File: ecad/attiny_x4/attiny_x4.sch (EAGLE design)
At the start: 1 part

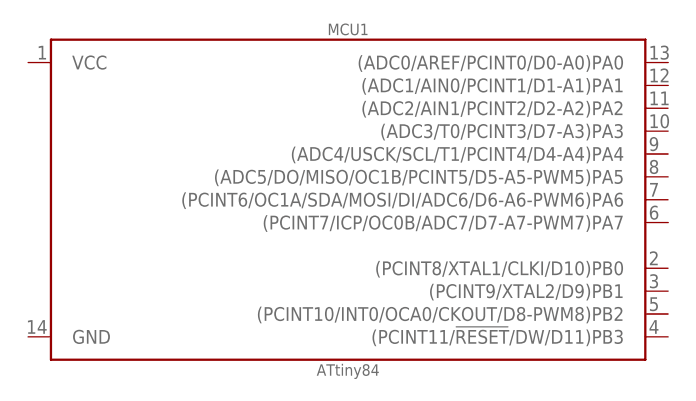
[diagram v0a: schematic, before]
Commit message: Update ATtiny84 symbol to match the CCW ATtiny core.
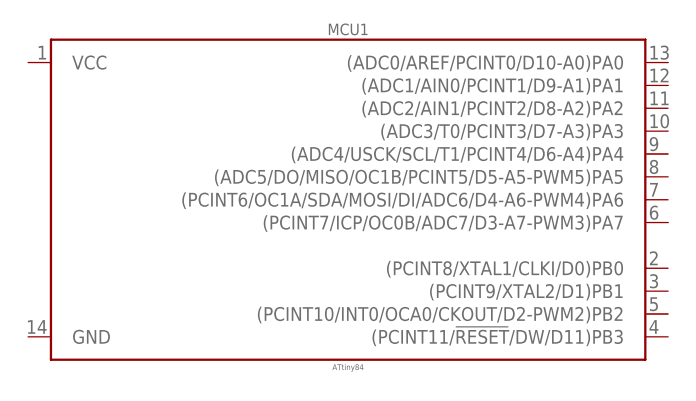
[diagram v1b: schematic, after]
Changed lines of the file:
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@@
 <instances>
 <instance part="MCU1" gate="G$1" x="50.8" y="30.48" smashed="yes">
-<attribute name="VALUE" x="50.8" y="12.192" size="1.27" layer="96" font="vector" ratio="10" align="top-center"/>
+<attribute name="VALUE" x="50.8" y="12.192" size="0.635" layer="96" font="vector" ratio="10" align="top-center"/>
 <attribute name="NAME" x="50.8" y="48.768" size="1.27" layer="95" font="vector" ratio="10" align="bottom-center"/>
 </instance>
